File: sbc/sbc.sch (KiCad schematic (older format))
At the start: 4 parts

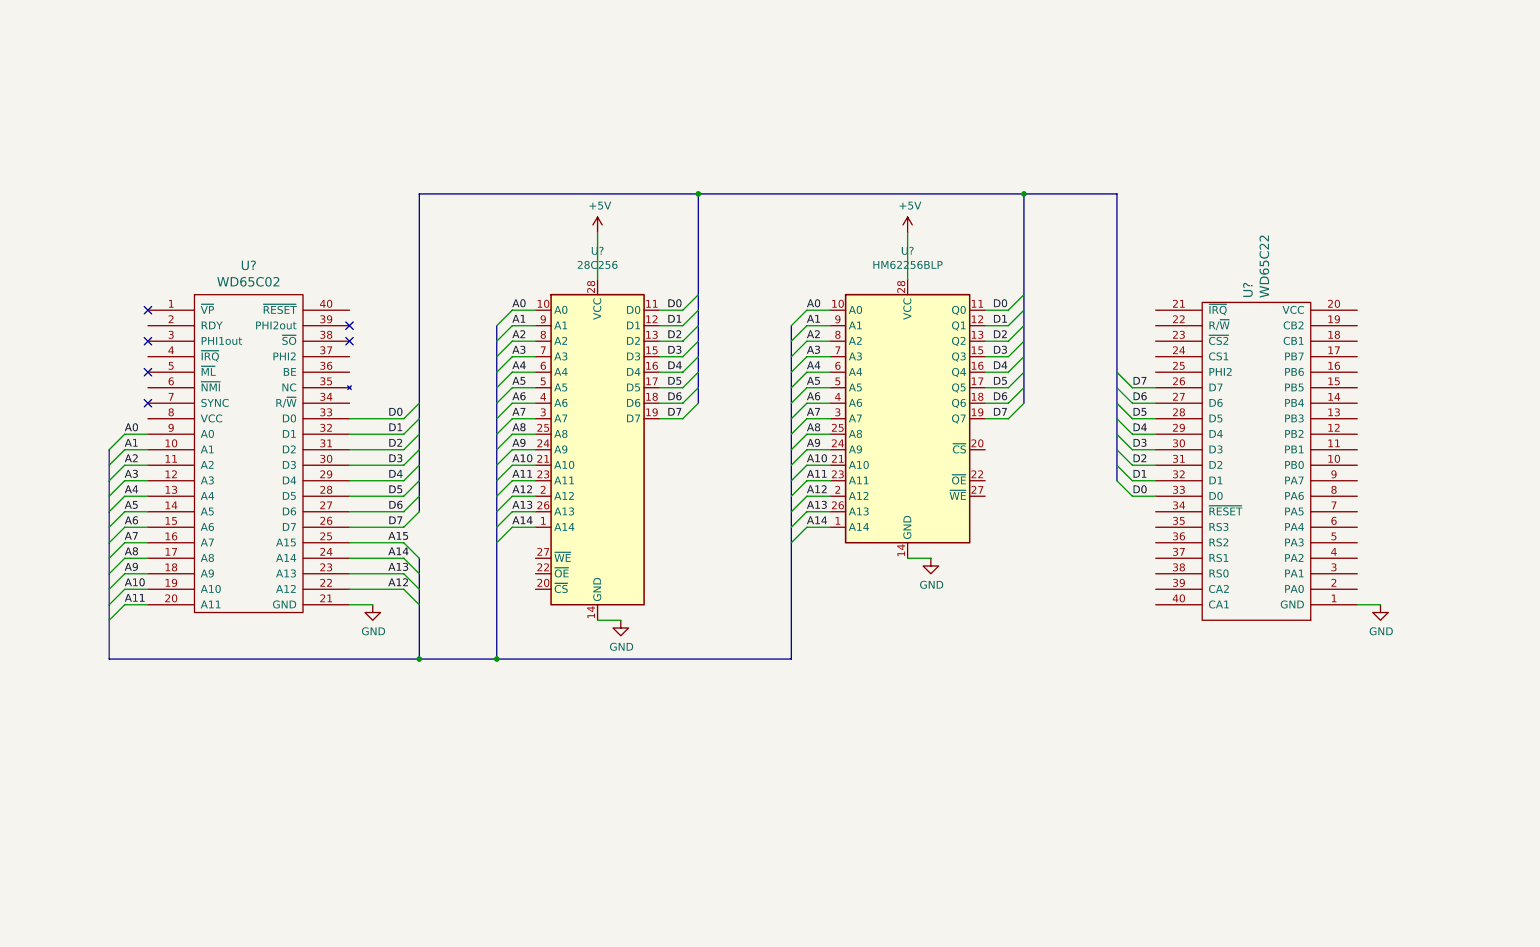
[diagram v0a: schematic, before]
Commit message: SBC: Wire up glue logic
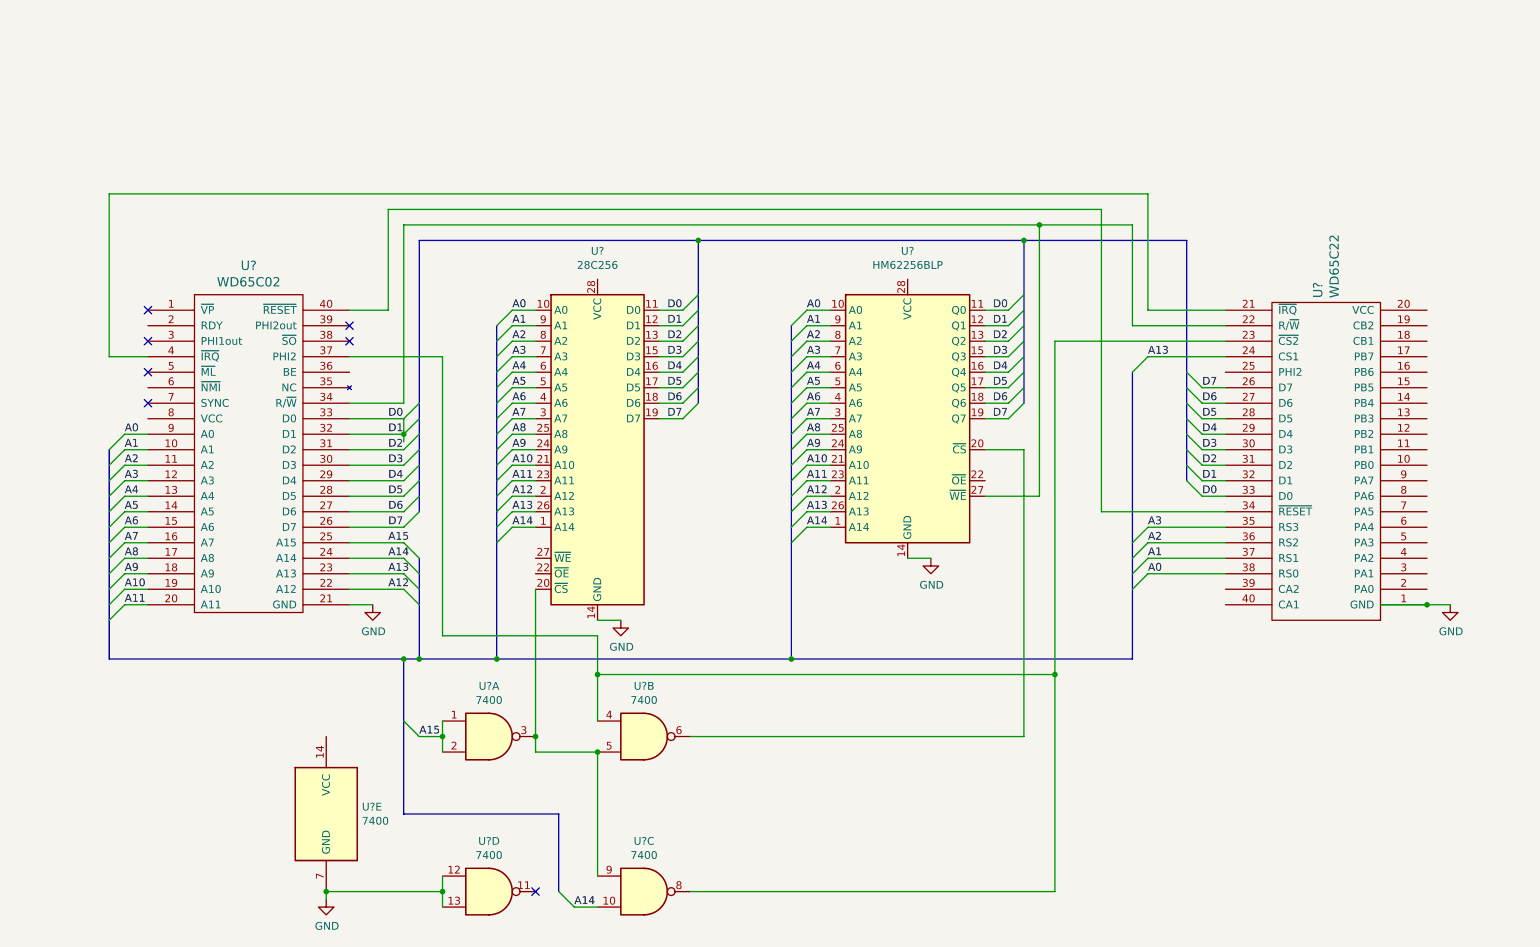
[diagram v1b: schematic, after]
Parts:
- added U? (x5): 7400, symbol 74xx:7400
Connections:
- net D1 is gone; now on net D0: U?.12 (D1), U?.12 (Q1), U?.32 (D1), U?.32 (D1)
- net A0: now also U?.38 (RS0)
- net A1: now also U?.37 (RS1)
- net A13: now also U?.24 (CS1)
- net A14: now also U?.10
- net A15: now also U?.1, U?.2
- net A2: now also U?.36 (RS2)
- net A3: now also U?.35 (RS3)
- net GND: now also U?.12, U?.13, U?.7 (GND)
- net at U?.34 (R/~W): now also U?.22 (R/~W), U?.27 (~WE)
- net at U?.37 (PHI2): now also U?.23 (~CS2), U?.4, U?.8
- net at U?.4 (~IRQ): now also U?.21 (~IRQ)
- net at U?.40 (~RESET): now also U?.34 (~RESET)
- net at U?.20 (~CS): now also U?.3, U?.5, U?.9
- net at U?.20 (~CS): now also U?.6
- net +5V: no longer names the net of U?.28 (VCC)
- net +5V: no longer U?.28 (VCC)
- no-connect marks 6 -> 7
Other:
- moved on the sheet: U?

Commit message: SBC: Wire up power
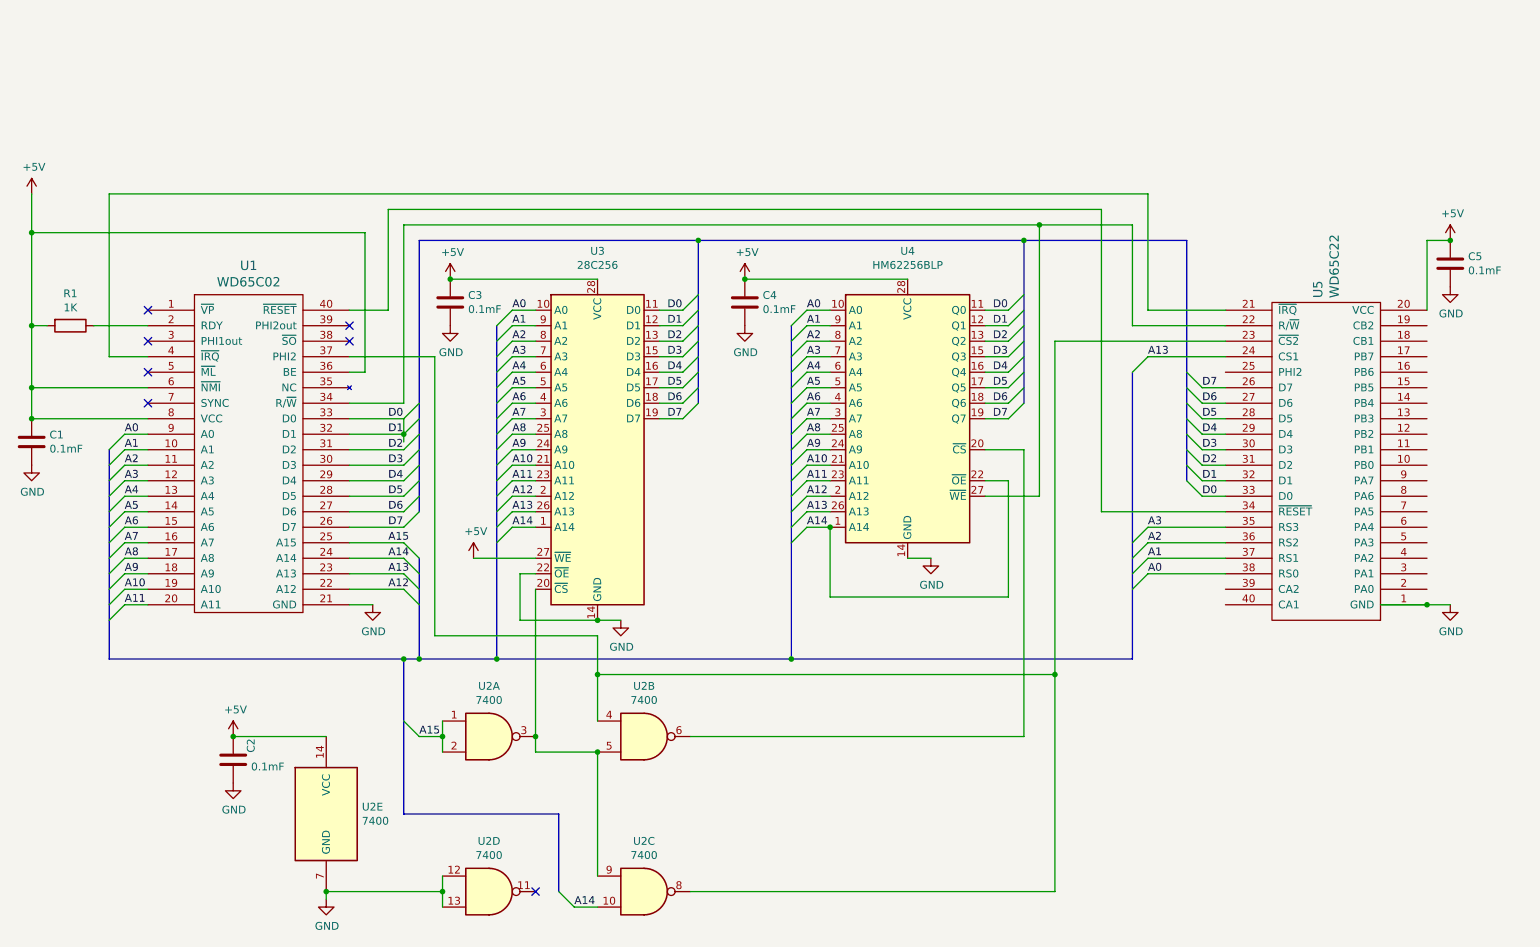
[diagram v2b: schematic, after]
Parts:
- added C1, C2, C3, C4, C5: 0.1mF, symbol device:C
- added R1: 1K, symbol device:R
- gave numbers to parts that had none: 5
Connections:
- net A14: now also U4.22 (~OE)
- net GND: now also U3.22 (~OE), C1.2, C2.2, C3.2, C4.2, C5.2
- net at U1.2 (RDY): now also R1.1
- net +5V: now reaches U1.36 (BE)
- net +5V: now also U1.6 (~NMI), U1.8 (VCC), U2.14 (VCC), U3.27 (~WE), U3.28 (VCC), U4.28 (VCC), U5.20 (VCC), C1.1, C2.1, C3.1, C4.1, C5.1, R1.2

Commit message: SBC: Wire up peripheral A and B connectors
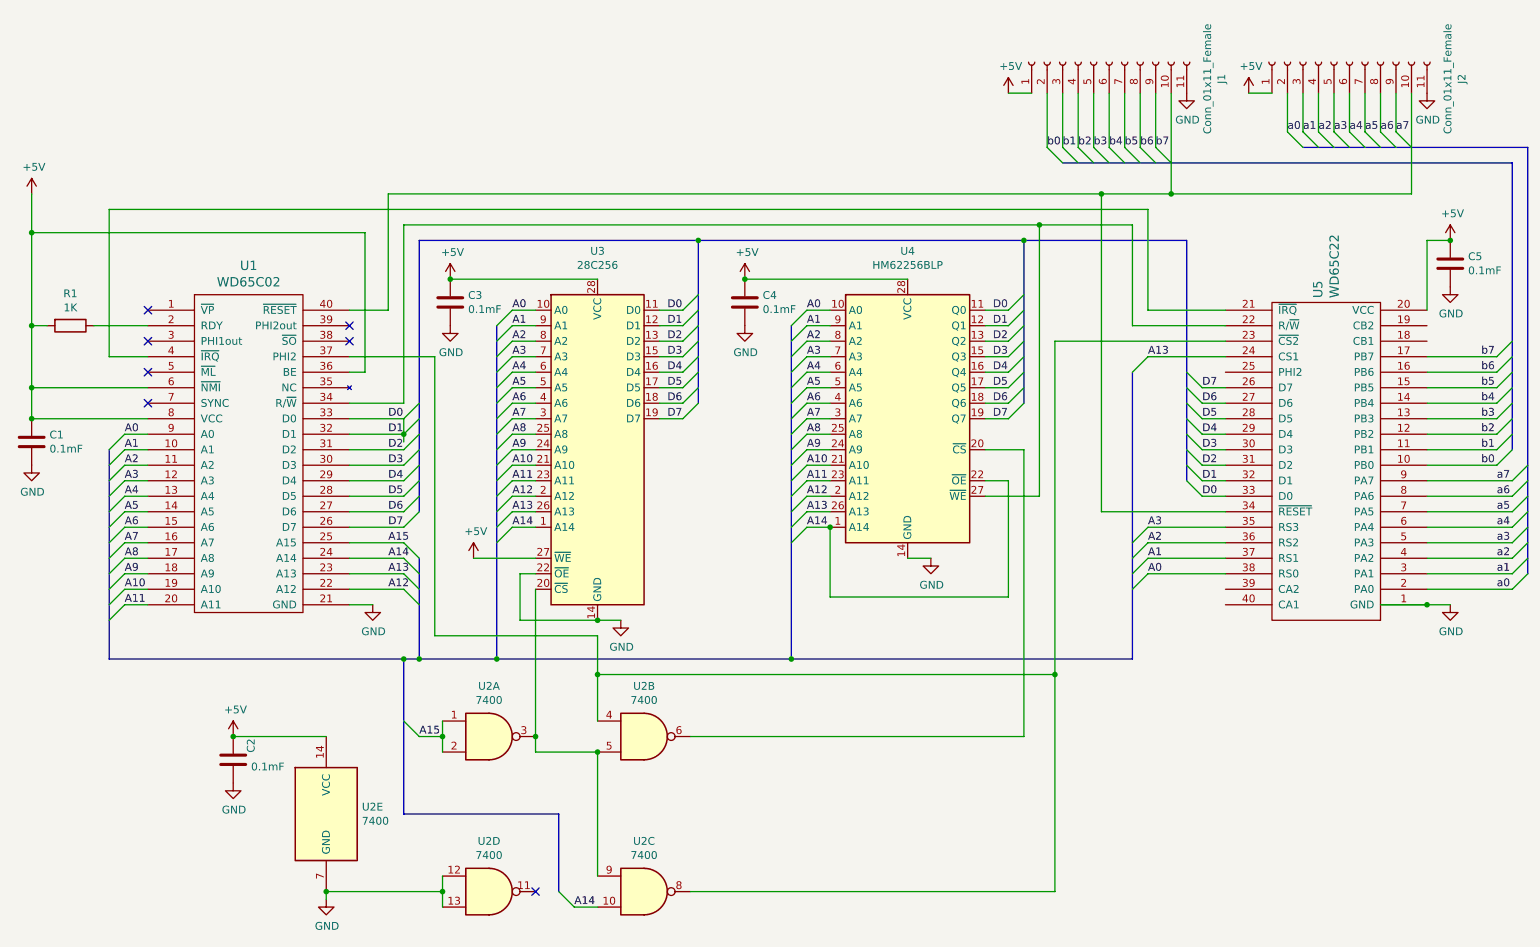
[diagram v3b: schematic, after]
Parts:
- added J1, J2: Conn_01x11_Female, symbol connector:Conn_01x11_Female
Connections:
- net +5V: now also J1.1 (Pin_1), J2.1 (Pin_1)
- net GND: now also J1.11 (Pin_11), J2.11 (Pin_11)
- net at U1.40 (~RESET), U5.34 (~RESET): now also J1.10 (Pin_10), J2.10 (Pin_10)
- net b0: now reaches U5.10 (PB0)
- net b0: now also J1.2 (Pin_2)
- net b1: now reaches U5.11 (PB1)
- net b1: now also J1.3 (Pin_3)
- net b2: now reaches U5.12 (PB2)
- net b2: now also J1.4 (Pin_4)
- net b3: now reaches U5.13 (PB3)
- net b3: now also J1.5 (Pin_5)
- net b4: now reaches U5.14 (PB4)
- net b4: now also J1.6 (Pin_6)
- net b5: now reaches U5.15 (PB5)
- net b5: now also J1.7 (Pin_7)
- net b6: now reaches U5.16 (PB6)
- net b6: now also J1.8 (Pin_8)
- net b7: now reaches U5.17 (PB7)
- net b7: now also J1.9 (Pin_9)
- net a0: now reaches U5.2 (PA0)
- net a0: now also J2.2 (Pin_2)
- net a1: now reaches U5.3 (PA1)
- net a1: now also J2.3 (Pin_3)
- net a2: now reaches U5.4 (PA2)
- net a2: now also J2.4 (Pin_4)
- net a3: now reaches U5.5 (PA3)
- net a3: now also J2.5 (Pin_5)
- net a4: now reaches U5.6 (PA4)
- net a4: now also J2.6 (Pin_6)
- net a5: now reaches U5.7 (PA5)
- net a5: now also J2.7 (Pin_7)
- net a6: now reaches U5.8 (PA6)
- net a6: now also J2.8 (Pin_8)
- net a7: now reaches U5.9 (PA7)
- net a7: now also J2.9 (Pin_9)

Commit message: SBC: Wire up oscillator
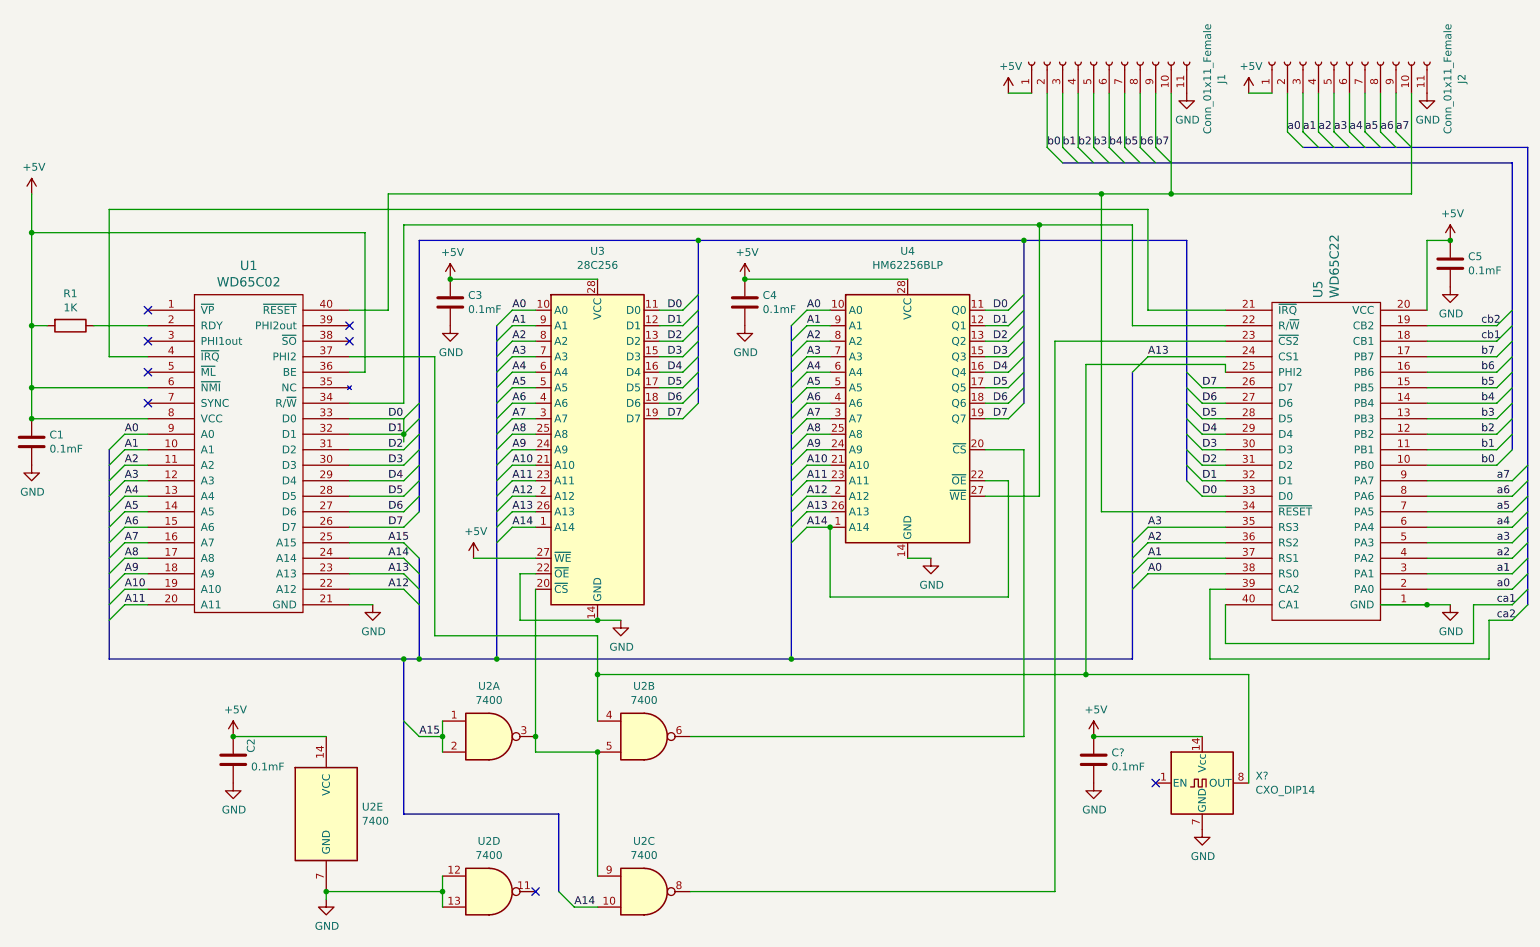
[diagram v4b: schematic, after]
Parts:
- added C?: 0.1mF, symbol device:C
- added X?: CXO_DIP14, Oscillator:Oscillator_DIP-14, symbol oscillator:CXO_DIP14
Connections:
- net +5V: now also C?.1, X?.14 (Vcc)
- net GND: now also C?.2, X?.7 (GND)
- net at U1.37 (PHI2), U2.4: now also U5.25 (PHI2), X?.8 (OUT); no longer U2.8, U5.23 (~CS2)
- net cb1: now reaches U5.18 (CB1)
- net cb2: now reaches U5.19 (CB2)
- net ca2: now reaches U5.39 (CA2)
- net ca1: now reaches U5.40 (CA1)
- new net: U2.8, U5.23 (~CS2)
- no-connect marks 7 -> 8
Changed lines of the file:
@@
 Wire Wire Line
 	7250 5250 5100 5250
-Wire Wire Line
-	5100 6250 7450 6250
-Wire Wire Line
-	7450 6250 7450 4850
 Connection ~ 5750 4750
-Wire Wire Line
-	4500 5150 4500 4850
 Wire Wire Line
 	3450 2800 2900 2800
@@
 Wire Wire Line
 	1350 2800 1600 2800
-Connection ~ 4500 4850
 NoConn ~ 4100 6250
 Wire Wire Line
@@
 Entry Wire Line
 	8050 4000 7950 4100
-Wire Wire Line
-	7450 4850 4500 4850
 Entry Wire Line
 	8400 3500 8300 3400
@@
 Wire Wire Line
 	8550 3700 8400 3700
-Wire Wire Line
-	7450 2700 8550 2700
 Wire Wire Line
 	8400 3600 8550 3600
@@
 Entry Wire Line
 	8050 2800 7950 2900
-Connection ~ 7450 4850
-Wire Wire Line
-	7450 4850 7450 2700
 $Comp
 L power:GND #PWR020
@@
 Wire Wire Line
 	3450 4600 3450 2800
-Wire Wire Line
-	4500 4850 4500 4600
 Wire Wire Line
 	4500 4600 3450 4600
@@
 Text Label 8950 1350 0    50   ~ 0
 a0
-Wire Wire Line
-	9750 1100 9750 1750
-Wire Wire Line
-	8200 1100 8200 1750
-Wire Bus Line
-	3250 4750 3250 5750
-Wire Bus Line
-	3350 4100 3350 4750
-Wire Bus Line
-	7950 2900 7950 4750
-Wire Bus Line
-	9050 1450 10500 1450
-Wire Bus Line
-	7500 1550 10400 1550
-Wire Bus Line
-	10500 1450 10500 4200
-Wire Bus Line
-	10400 1550 10400 3400
-Wire Bus Line
-	8300 2050 8300 3600
-Wire Bus Line
-	7250 2050 7250 3100
-Wire Bus Line
-	5150 2050 5150 3100
-Wire Bus Line
-	3350 2050 3350 3800
-Wire Bus Line
-	1350 3400 1350 4750
-Wire Bus Line
-	3850 2600 3850 4750
-Wire Bus Line
-	5750 2600 5750 4750
 Text Label 9050 1350 0    50   ~ 0
 a1
@@
 Text Label 8100 1450 0    50   ~ 0
 b7
+Wire Wire Line
+	4500 4600 4500 4850
+Connection ~ 4500 4850
+Wire Wire Line
+	4500 4850 4500 5150
+Wire Wire Line
+	5100 6250 7450 6250
+Wire Wire Line
+	7450 2700 8550 2700
+Wire Wire Line
+	7450 2700 7450 6250
+Wire Wire Line
+	8550 2900 8550 2850
+Wire Wire Line
+	8550 2850 7650 2850
+Wire Wire Line
+	7650 2850 7650 4850
+Wire Wire Line
+	4500 4850 7650 4850
+$Comp
+L oscillator:CXO_DIP14 X?
+U 1 1 61142AF5
+P 8400 5550
+F 0 "X?" H 8744 5596 50  0000 L CNN
+F 1 "CXO_DIP14" H 8744 5505 50  0000 L CNN
+F 2 "Oscillator:Oscillator_DIP-14" H 8850 5200 50  0001 C CNN
+F 3 "http://cdn-reichelt.de/documents/datenblatt/B400/OSZI.pdf" H 8300 5550 50  0001 C CNN
+	1    8400 5550
+	1    0    0    -1
+$EndComp
+$Comp
+L power:GND #PWR?
+U 1 1 6117B29B
+P 8400 5850
+F 0 "#PWR?" H 8400 5600 50  0001 C CNN
+F 1 "GND" H 8405 5677 50  0000 C CNN
+F 2 "" H 8400 5850 50  0001 C CNN
+F 3 "" H 8400 5850 50  0001 C CNN
+	1    8400 5850
+	1    0    0    -1
+$EndComp
+$Comp
+L device:C C?
+U 1 1 6119EE14
+P 7700 5400
+F 0 "C?" H 7815 5446 50  0000 L CNN
+F 1 "0.1mF" H 7815 5355 50  0000 L CNN
+F 2 "" H 7738 5250 50  0001 C CNN
+F 3 "~" H 7700 5400 50  0001 C CNN
+	1    7700 5400
+	1    0    0    -1
+$EndComp
+Wire Wire Line
+	8400 5250 7700 5250
+$Comp
+L power:GND #PWR?
+U 1 1 611DB51B
+P 7700 5550
+F 0 "#PWR?" H 7700 5300 50  0001 C CNN
+F 1 "GND" H 7705 5377 50  0000 C CNN
+F 2 "" H 7700 5550 50  0001 C CNN
+F 3 "" H 7700 5550 50  0001 C CNN
+	1    7700 5550
+	1    0    0    -1
+$EndComp
+$Comp
+L power:+5V #PWR?
+U 1 1 611DB960
+P 7700 5250
+F 0 "#PWR?" H 7700 5100 50  0001 C CNN
+F 1 "+5V" H 7715 5423 50  0000 C CNN
+F 2 "" H 7700 5250 50  0001 C CNN
+F 3 "" H 7700 5250 50  0001 C CNN
+	1    7700 5250
+	1    0    0    -1
+$EndComp
+Connection ~ 7700 5250
+NoConn ~ 8100 5550
+Wire Wire Line
+	8700 5550 8700 4850
+Wire Wire Line
+	8700 4850 7650 4850
+Connection ~ 7650 4850
+Entry Wire Line
+	10300 2700 10400 2600
+Entry Wire Line
+	10300 2600 10400 2500
+Wire Wire Line
+	10300 2600 9850 2600
+Wire Wire Line
+	10300 2700 9850 2700
+Text Label 10200 2600 0    50   ~ 0
+cb2
+Text Label 10200 2700 0    50   ~ 0
+cb1
+Entry Wire Line
+	10400 4400 10500 4300
+Entry Wire Line
+	10400 4500 10500 4400
+Wire Wire Line
+	8550 4400 8550 4650
+Wire Wire Line
+	8550 4650 10150 4650
+Wire Wire Line
+	10150 4650 10150 4400
+Wire Wire Line
+	10150 4400 10400 4400
+Wire Wire Line
+	8550 4300 8450 4300
+Wire Wire Line
+	8450 4300 8450 4750
+Wire Wire Line
+	8450 4750 10250 4750
+Text Label 10300 4400 0    50   ~ 0
+ca1
+Wire Wire Line
+	10400 4500 10250 4500
+Wire Wire Line
+	10250 4500 10250 4750
+Wire Wire Line
+	9750 1100 9750 1750
+Wire Wire Line
+	8200 1100 8200 1750
+Wire Bus Line
+	3250 4750 3250 5750
+Wire Bus Line
+	3350 4100 3350 4750
+Wire Bus Line
+	7950 2900 7950 4750
+Wire Bus Line
+	10400 1550 10400 3400
+Wire Bus Line
+	9050 1450 10500 1450
+Wire Bus Line
+	7500 1550 10400 1550
+Wire Bus Line
+	10500 1450 10500 4400
+Wire Bus Line
+	8300 2050 8300 3600
+Wire Bus Line
+	7250 2050 7250 3100
+Wire Bus Line
+	5150 2050 5150 3100
+Wire Bus Line
+	3350 2050 3350 3800
+Wire Bus Line
+	1350 3400 1350 4750
+Wire Bus Line
+	3850 2600 3850 4750
+Wire Bus Line
+	5750 2600 5750 4750
+Text Label 10300 4500 0    50   ~ 0
+ca2
 $EndSCHEMATC
